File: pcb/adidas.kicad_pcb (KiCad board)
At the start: 2 copper layers, 152.7 x 107.2 mm, 34 parts, among them J1 ISP Header, J2 Shitty Add-on, J4 Battery, U1 MPU-6050, U2 ATTINY841-SSU

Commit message: RUN DRC v0.2 (#25)
* refactor

* RUN DRC

* cleanup for v0.2

* final v0.2
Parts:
- J4: value Battery -> мощность
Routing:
- net GND: track 0.00 -> 367.1 mm, vias 0 -> 2
- net /7(SDA): track 0.00 -> 189.3 mm
- net /4(RST): track 0.00 -> 169.9 mm
- net /9(SCL): track 0.00 -> 167.8 mm, vias 0 -> 2
- net VCC: track 0.00 -> 149.7 mm
- net /3(LED Mid Row): track 0.00 -> 127.5 mm
- net Net-(D8-Pad2): track 0.00 -> 124.8 mm, vias 0 -> 1
- net Net-(J1-Pin_1): track 0.00 -> 121.6 mm, vias 0 -> 1
- net /2(LED Bottom Row): track 0.00 -> 101.6 mm
- net Net-(D4-Pad2): track 0.00 -> 100.2 mm, vias 0 -> 1
- net /13(SAO1): track 0.00 -> 92.9 mm, vias 0 -> 1
- net /12(SAO2): track 0.00 -> 90.5 mm, vias 0 -> 2
- net /5(LED Top Row): track 0.00 -> 88.3 mm, vias 0 -> 2
- net Net-(D1-Pad2): track 0.00 -> 71.6 mm, vias 0 -> 1
- net +BATT: track 0.00 -> 59.2 mm
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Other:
- board text added: "SCL"
- board text added: "SDA"
- board text added: "THE @DEAD10C5 LOVE YOU!! @p0lr_ - Eddie the Yeti yaya_pancho - @thedevilsvoice"
- board text removed: "MISO"
- board text removed: "MOSI"
- board text removed: "SCK"
- board text removed: "THE @DEAD10C5 LOVE YOU!! @p0lr_ - Eddie the Yeti yaya_pancho - @5l0w0n3 @thedevilsvoice"

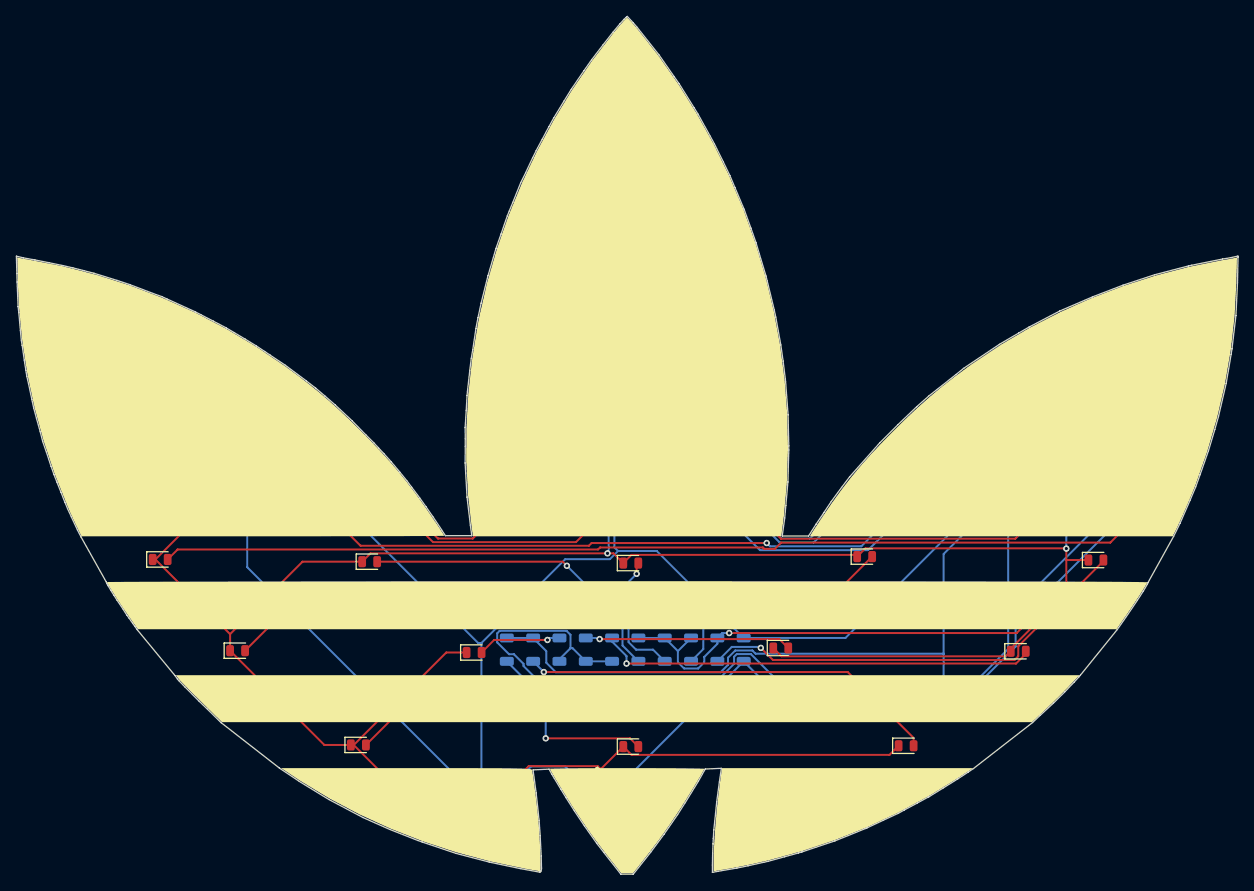
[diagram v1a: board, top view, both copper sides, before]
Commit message: make some changes from PCBway feedback v0.3
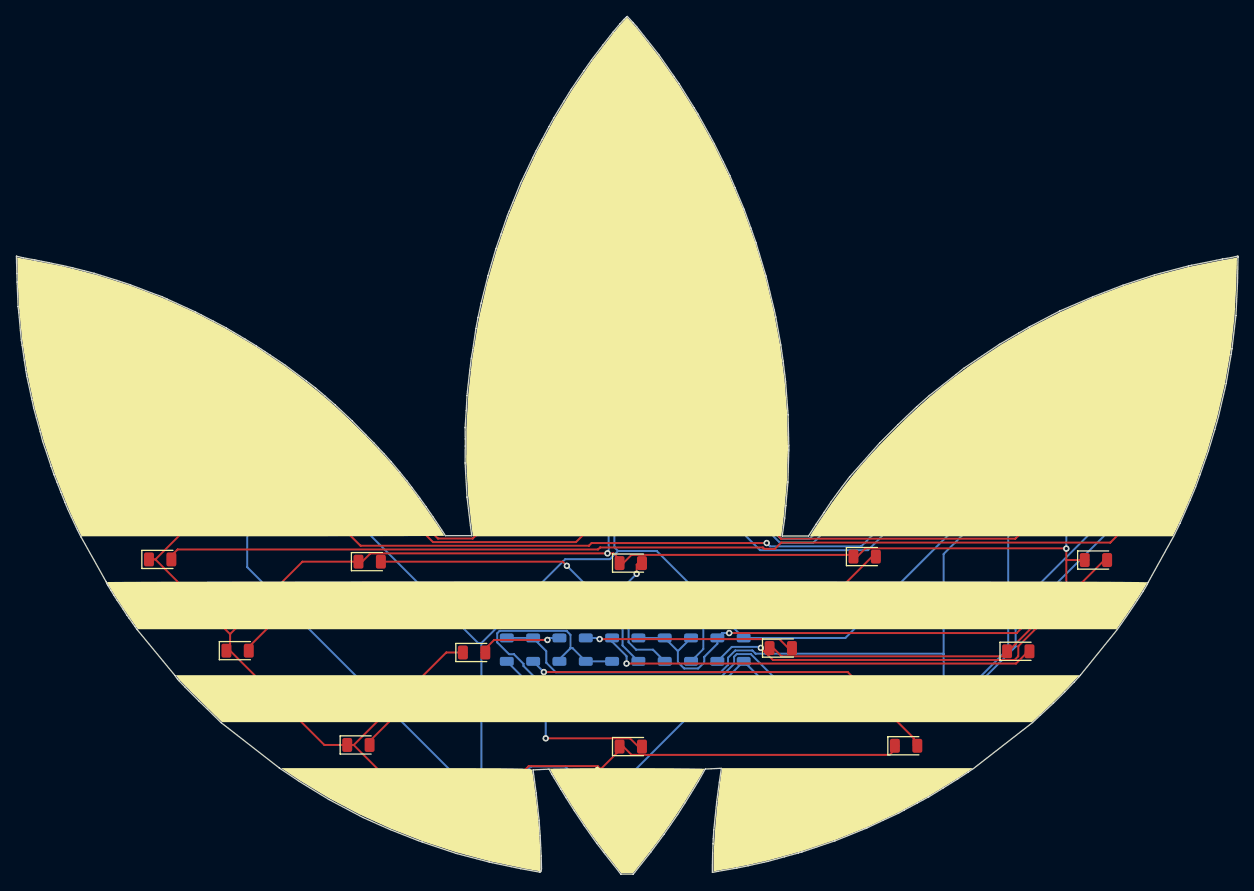
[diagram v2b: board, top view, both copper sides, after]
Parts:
- removed BT1: Battery_Cell, Battery:BatteryHolder_Keystone_3002_1x2032
- removed REF**: MountingHole_4.5mm, MountingHole:MountingHole_4.5mm
- D1, D10, D12, D2, D3, D4, D5, D6, D7, D8, D9: value LHN974 -> AP3216SYCK; footprint LED_SMD:LED_0805_2012Metric -> LED_SMD:LED_1206_3216Metric
- D11: value ~ -> AP3216SYCK; footprint LED_SMD:LED_0805_2012Metric -> LED_SMD:LED_1206_3216Metric
- J4: value мощность -> Battery
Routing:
- net +BATT: track 59.2 -> 0.00 mm
- net (no net): track 0.00 -> 59.2 mm

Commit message: add mouser and digikey part numbers
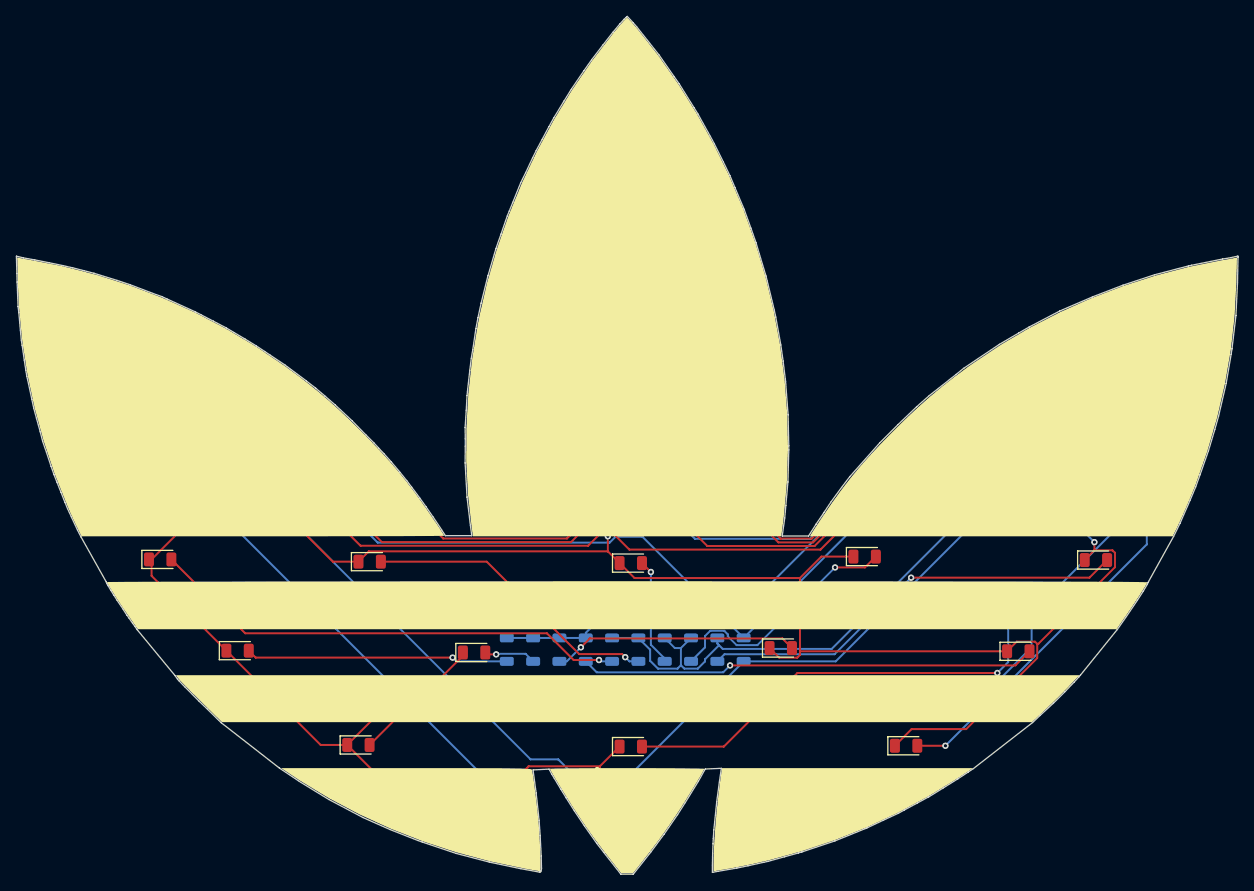
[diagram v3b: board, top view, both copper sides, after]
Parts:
- D1, D10, D11, D12, D2, D3, D4, D5, D6, D7, D8, D9: value AP3216SYCK -> CTL1206FWH1T
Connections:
- R2 pad 1: Net-(D4-Pad2) -> /2(LED Bottom Row)
- R2 pad 2: /3(LED Mid Row) -> Net-(D2-Pad2)
- R3 pad 1: /5(LED Top Row) -> /2(LED Bottom Row)
- R3 pad 2: Net-(D8-Pad2) -> Net-(D3-Pad2)
- R4 pad 1: /2(LED Bottom Row) -> /3(LED Mid Row)
- R4 pad 2: Net-(D2-Pad2) -> Net-(D4-Pad2)
- R5 pad 1: /2(LED Bottom Row) -> /3(LED Mid Row)
- R5 pad 2: Net-(D3-Pad2) -> Net-(D5-Pad2)
- R6 pad 1: Net-(D5-Pad2) -> /3(LED Mid Row)
- R6 pad 2: /3(LED Mid Row) -> Net-(D6-Pad2)
- R7 pad 1: Net-(D6-Pad2) -> /3(LED Mid Row)
- R7 pad 2: /3(LED Mid Row) -> Net-(D7-Pad2)
- R8 pad 1: Net-(D7-Pad2) -> /5(LED Top Row)
- R8 pad 2: /3(LED Mid Row) -> Net-(D8-Pad2)
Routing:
- net Net-(D4-Pad2): track 100.2 -> 32.8 mm
- net Net-(D8-Pad2): track 124.8 -> 60.4 mm
- net (no net): track 59.2 -> 0.00 mm
- net /2(LED Bottom Row): track 101.6 -> 51.9 mm
- net /3(LED Mid Row): track 127.5 -> 92.7 mm, vias 0 -> 2
- net Net-(D2-Pad2): track 23.6 -> 56.2 mm
- net VCC: track 149.7 -> 179.4 mm
- net /7(SDA): track 189.3 -> 161.3 mm, vias 0 -> 1
- net /4(RST): track 169.9 -> 147.6 mm
- net GND: track 367.1 -> 347.2 mm
- net Net-(D3-Pad2): track 52.5 -> 42.6 mm
- net Net-(J1-Pin_1): track 121.6 -> 116.4 mm
- net Net-(D6-Pad2): track 25.8 -> 30.7 mm
- net Net-(D5-Pad2): track 10.5 -> 6.50 mm
- net Net-(D7-Pad2): track 54.7 -> 57.1 mm
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
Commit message: run ERC checks
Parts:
- D1, D10, D11, D12, D2, D3, D4, D5, D6, D7, D8, D9: value CTL1206FWH1T -> AP3216SYCK
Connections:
- R2 pad 1: /2(LED Bottom Row) -> Net-(D4-Pad2)
- R2 pad 2: Net-(D2-Pad2) -> /3(LED Mid Row)
- R3 pad 1: /2(LED Bottom Row) -> /5(LED Top Row)
- R3 pad 2: Net-(D3-Pad2) -> Net-(D8-Pad2)
- R4 pad 1: /3(LED Mid Row) -> /2(LED Bottom Row)
- R4 pad 2: Net-(D4-Pad2) -> Net-(D2-Pad2)
- R5 pad 1: /3(LED Mid Row) -> /2(LED Bottom Row)
- R5 pad 2: Net-(D5-Pad2) -> Net-(D3-Pad2)
- R6 pad 1: /3(LED Mid Row) -> Net-(D5-Pad2)
- R6 pad 2: Net-(D6-Pad2) -> /3(LED Mid Row)
- R7 pad 1: /3(LED Mid Row) -> Net-(D6-Pad2)
- R7 pad 2: Net-(D7-Pad2) -> /3(LED Mid Row)
- R8 pad 1: /5(LED Top Row) -> Net-(D7-Pad2)
- R8 pad 2: Net-(D8-Pad2) -> /3(LED Mid Row)
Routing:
- net Net-(D4-Pad2): track 32.8 -> 100.2 mm
- net Net-(D8-Pad2): track 60.4 -> 124.8 mm
- net (no net): track 0.00 -> 59.2 mm
- net /2(LED Bottom Row): track 51.9 -> 101.6 mm
- net /3(LED Mid Row): track 92.7 -> 127.5 mm, vias 2 -> 0
- net Net-(D2-Pad2): track 56.2 -> 23.6 mm
- net VCC: track 179.4 -> 149.7 mm
- net /7(SDA): track 161.3 -> 189.3 mm, vias 1 -> 0
- net /4(RST): track 147.6 -> 169.9 mm
- net GND: track 347.2 -> 367.1 mm
- net Net-(D3-Pad2): track 42.6 -> 52.5 mm
- net Net-(J1-Pin_1): track 116.4 -> 121.6 mm
- net Net-(D6-Pad2): track 30.7 -> 25.8 mm
- net Net-(D5-Pad2): track 6.50 -> 10.5 mm
- net Net-(D7-Pad2): track 57.1 -> 54.7 mm
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
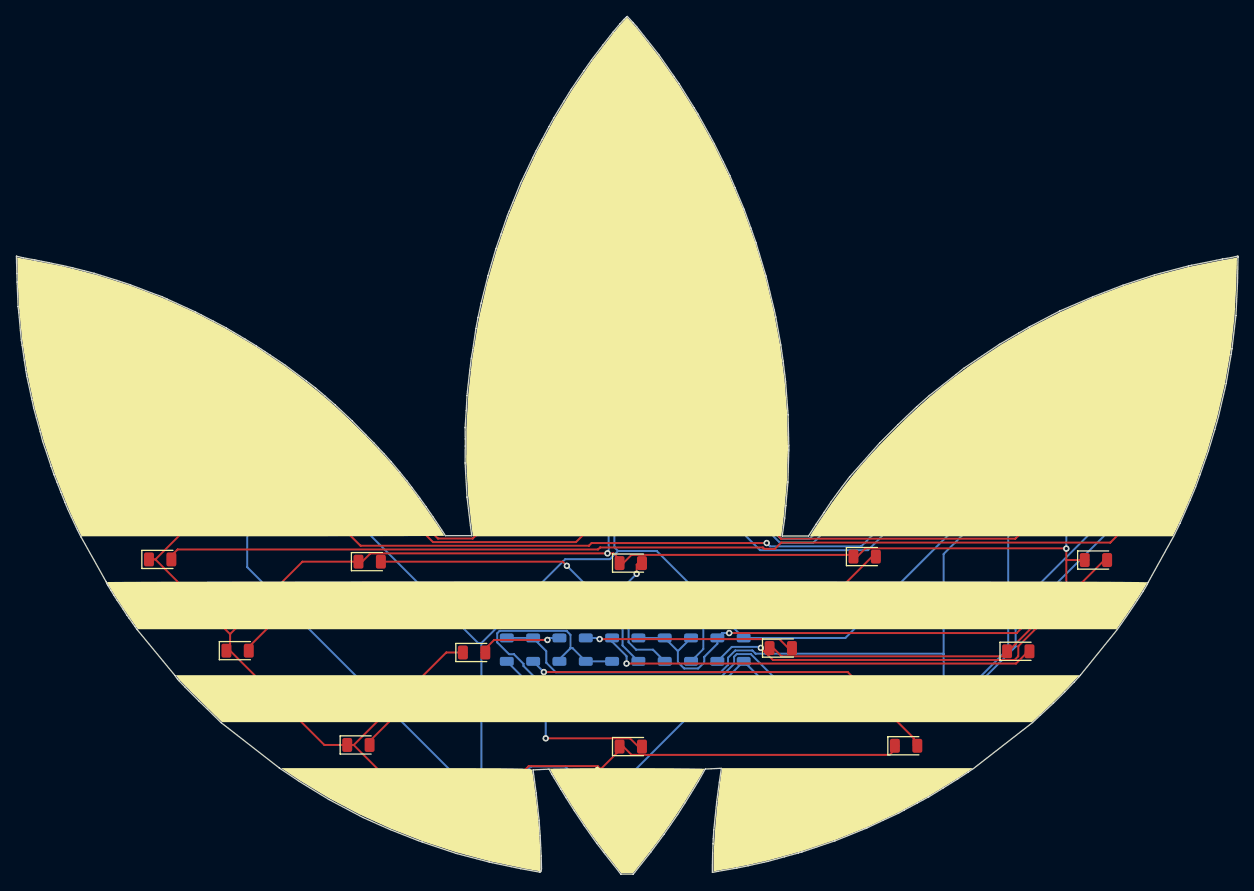
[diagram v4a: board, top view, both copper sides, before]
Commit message: update schematic
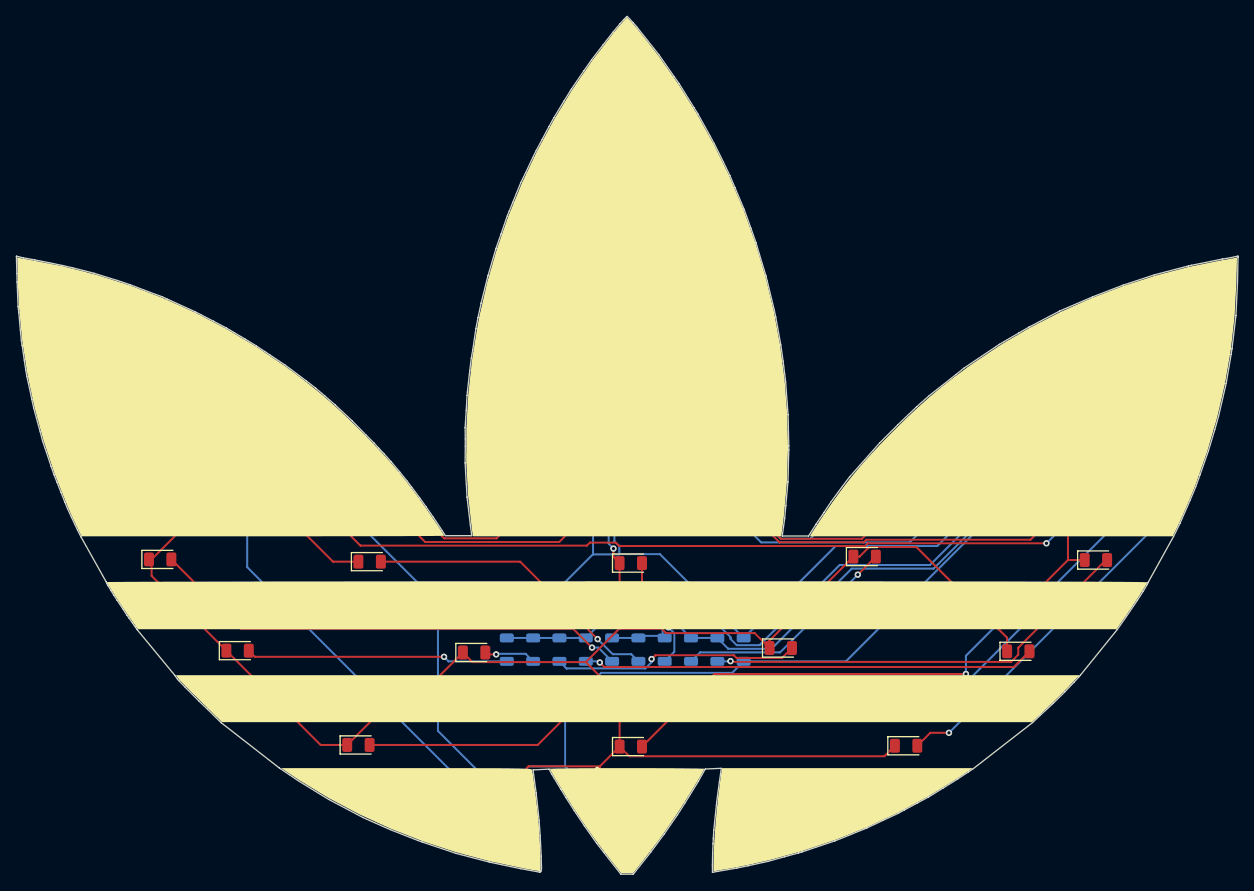
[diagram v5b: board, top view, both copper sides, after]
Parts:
- added REF**: MountingHole_4.5mm, DEAD10C5:MountingHole_4.5mm, F.Cu at (164.9, 48.1)
- D1, D10, D11, D12, D2, D3, D4, D5, D6, D7, D8, D9: value AP3216SYCK -> CTL1206FWH1T
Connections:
- J1 pad 2: VCC -> VDD
- J2 pad 1: VCC +3.3V -> VDD
- J4 pad 1: VCC -> VDD
- R13 pad 1: VCC -> VDD
- R2 pad 1: Net-(D4-Pad2) -> /2(LED Bottom Row)
- R2 pad 2: /3(LED Mid Row) -> Net-(D2-Pad2)
- R3 pad 1: /5(LED Top Row) -> /2(LED Bottom Row)
- R3 pad 2: Net-(D8-Pad2) -> Net-(D3-Pad2)
- R4 pad 1: /2(LED Bottom Row) -> /3(LED Mid Row)
- R4 pad 2: Net-(D2-Pad2) -> Net-(D4-Pad2)
- R5 pad 1: /2(LED Bottom Row) -> /3(LED Mid Row)
- R5 pad 2: Net-(D3-Pad2) -> Net-(D5-Pad2)
- R6 pad 1: Net-(D5-Pad2) -> /3(LED Mid Row)
- R6 pad 2: /3(LED Mid Row) -> Net-(D6-Pad2)
- R7 pad 1: Net-(D6-Pad2) -> /3(LED Mid Row)
- R7 pad 2: /3(LED Mid Row) -> Net-(D7-Pad2)
- R8 pad 1: Net-(D7-Pad2) -> /5(LED Top Row)
- R8 pad 2: /3(LED Mid Row) -> Net-(D8-Pad2)
- U1 pad 13: VCC -> VDD
- U2 pad 1: VCC -> VDD
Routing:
- net VDD: track 0.00 -> 204.9 mm
- net VCC: track 149.7 -> 0.00 mm
- net Net-(D4-Pad2): track 100.2 -> 32.8 mm
- net Net-(D8-Pad2): track 124.8 -> 60.4 mm
- net (no net): track 59.2 -> 0.00 mm
- net /2(LED Bottom Row): track 101.6 -> 54.5 mm
- net /3(LED Mid Row): track 127.5 -> 87.6 mm
- net GND: track 367.1 -> 328.7 mm
- net /9(SCL): track 167.8 -> 200.0 mm, vias 2 -> 1
- net Net-(D2-Pad2): track 23.6 -> 54.0 mm
- net /7(SDA): track 189.3 -> 161.2 mm, vias 0 -> 1
- net Net-(D3-Pad2): track 52.5 -> 41.9 mm
- net /5(LED Top Row): track 88.3 -> 78.0 mm, vias 2 -> 0
- net Net-(J1-Pin_1): track 121.6 -> 114.0 mm
- net Net-(D6-Pad2): track 25.8 -> 31.0 mm
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
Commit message: update schematic
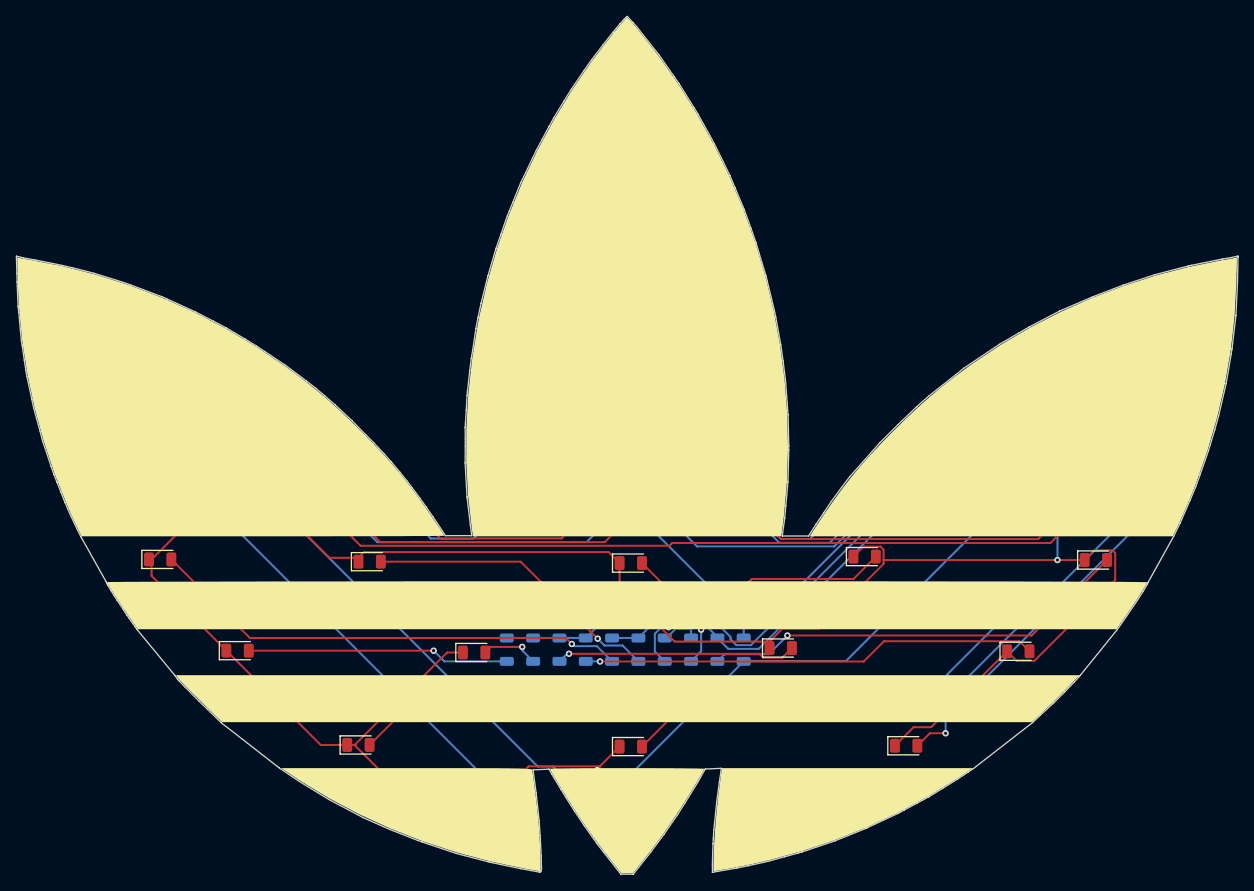
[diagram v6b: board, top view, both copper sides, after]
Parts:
- added BT1: Battery_Cell, DEAD10C5:BatteryHolder_Keystone_3002_1x2032, B.Cu at (165.4, 82.8)
- moved REF** 0.14 mm to (165.0, 48.2)
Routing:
- net GND: track 328.7 -> 428.9 mm, vias 2 -> 1
- net /9(SCL): track 200.0 -> 164.1 mm, vias 1 -> 2
- net VDD: track 204.9 -> 225.6 mm
- net /4(RST): track 167.1 -> 151.6 mm
- net /7(SDA): track 161.2 -> 170.3 mm, vias 1 -> 2
- net /5(LED Top Row): track 78.0 -> 80.6 mm
- net Net-(D11-Pad2): track 28.5 -> 30.1 mm
- net Net-(D10-Pad2): track 14.5 -> 15.4 mm
- net Net-(D6-Pad2): track 31.0 -> 30.2 mm
- net Net-(D5-Pad2): track 6.50 -> 7.28 mm
- net Net-(D12-Pad2): track 54.5 -> 54.0 mm
- net /12(SAO2): track 91.0 -> 91.1 mm, vias 1 -> 2
